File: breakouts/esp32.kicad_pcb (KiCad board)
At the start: 2 copper layers, 21.2 x 61.9 mm, 3 parts

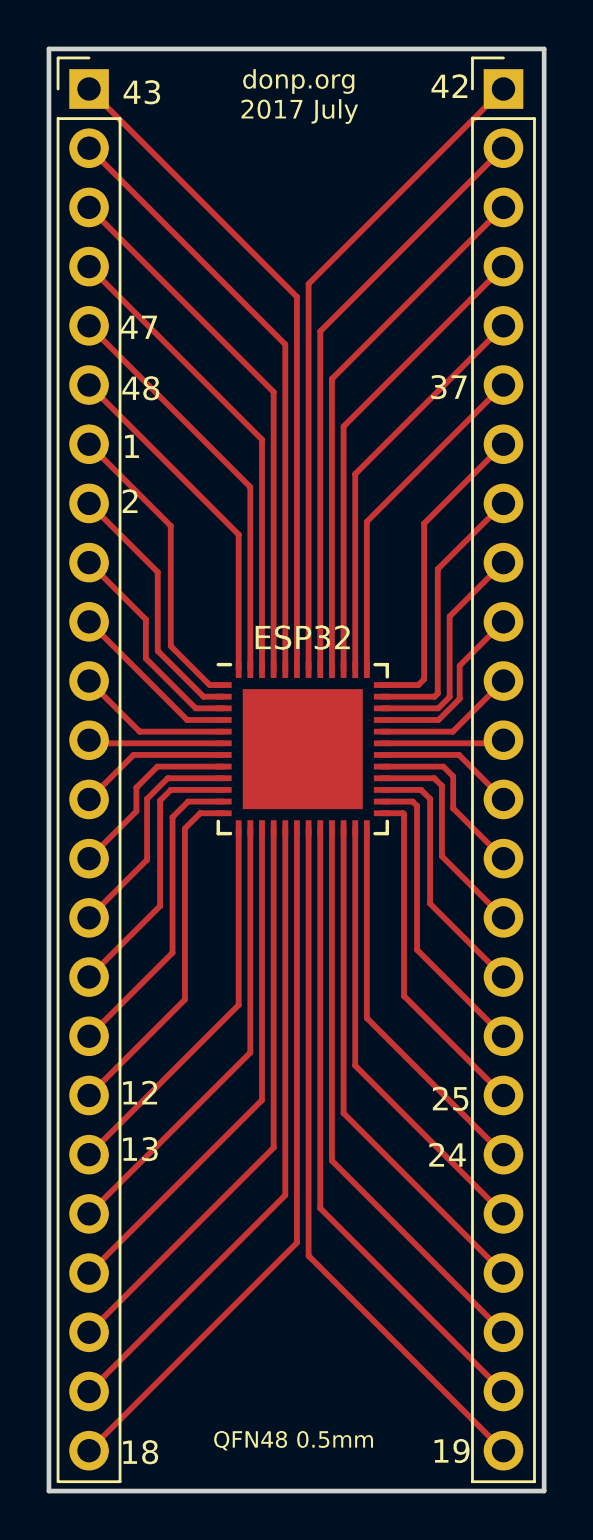
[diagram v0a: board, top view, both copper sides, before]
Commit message: qfn48 6x6
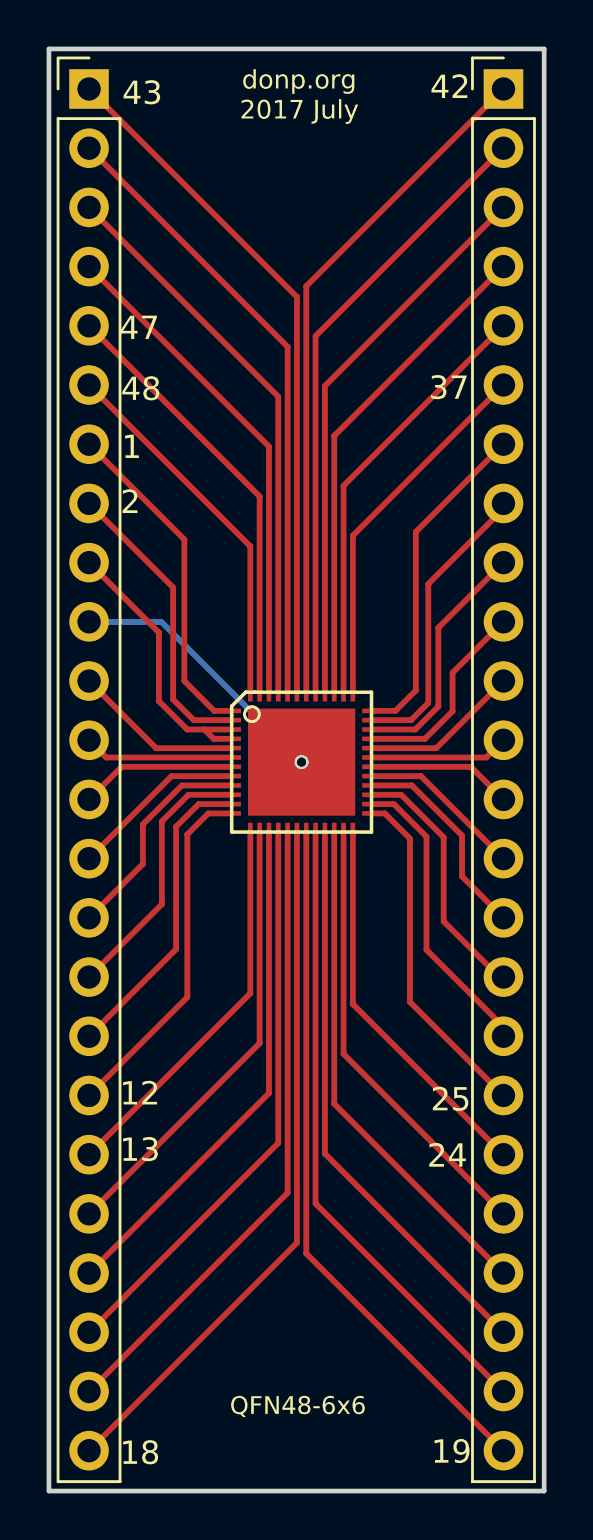
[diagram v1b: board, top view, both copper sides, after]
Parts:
- removed ESP32: QFN-48-1EP_7x7mm_Pitch0.5mm, Housings_DFN_QFN:QFN-48-1EP_7x7mm_Pitch0.5mm
- added QFN48-6x6: VAL**, tom_kicad_lib:QFN48+1, F.Cu at (136.1, 84.8)
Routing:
- net (no net): track 774.9 -> 801.7 mm, vias 0 -> 1
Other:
- board text removed: "QFN48 0.5mm"
